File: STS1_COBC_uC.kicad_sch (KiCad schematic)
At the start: 46 parts, among them J16 SWD, U18 STWD100PYW83F, U19 STM32F411RET6TR, U28 MCP130T-300I_TT, U29 74LVC1G08GV,125, U31 74LVC1G08GV,125, U32 74LVC1G32GV,125, Y1 12M

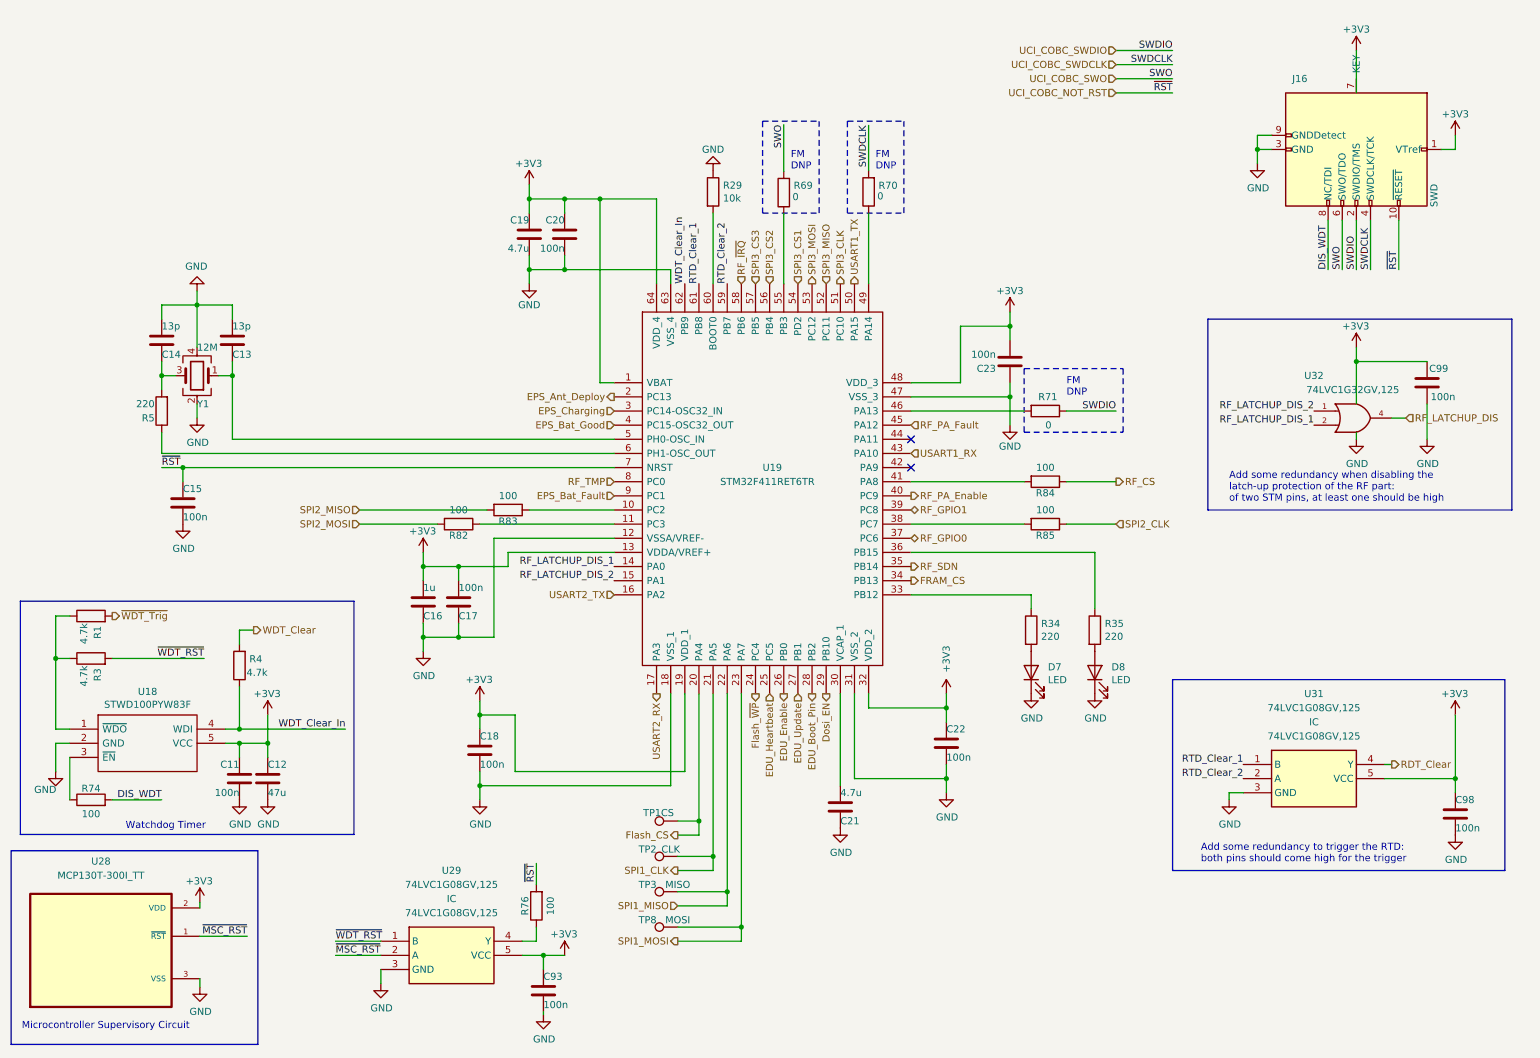
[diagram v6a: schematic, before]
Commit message: Fix power domain crossing issue between COBC and EPS
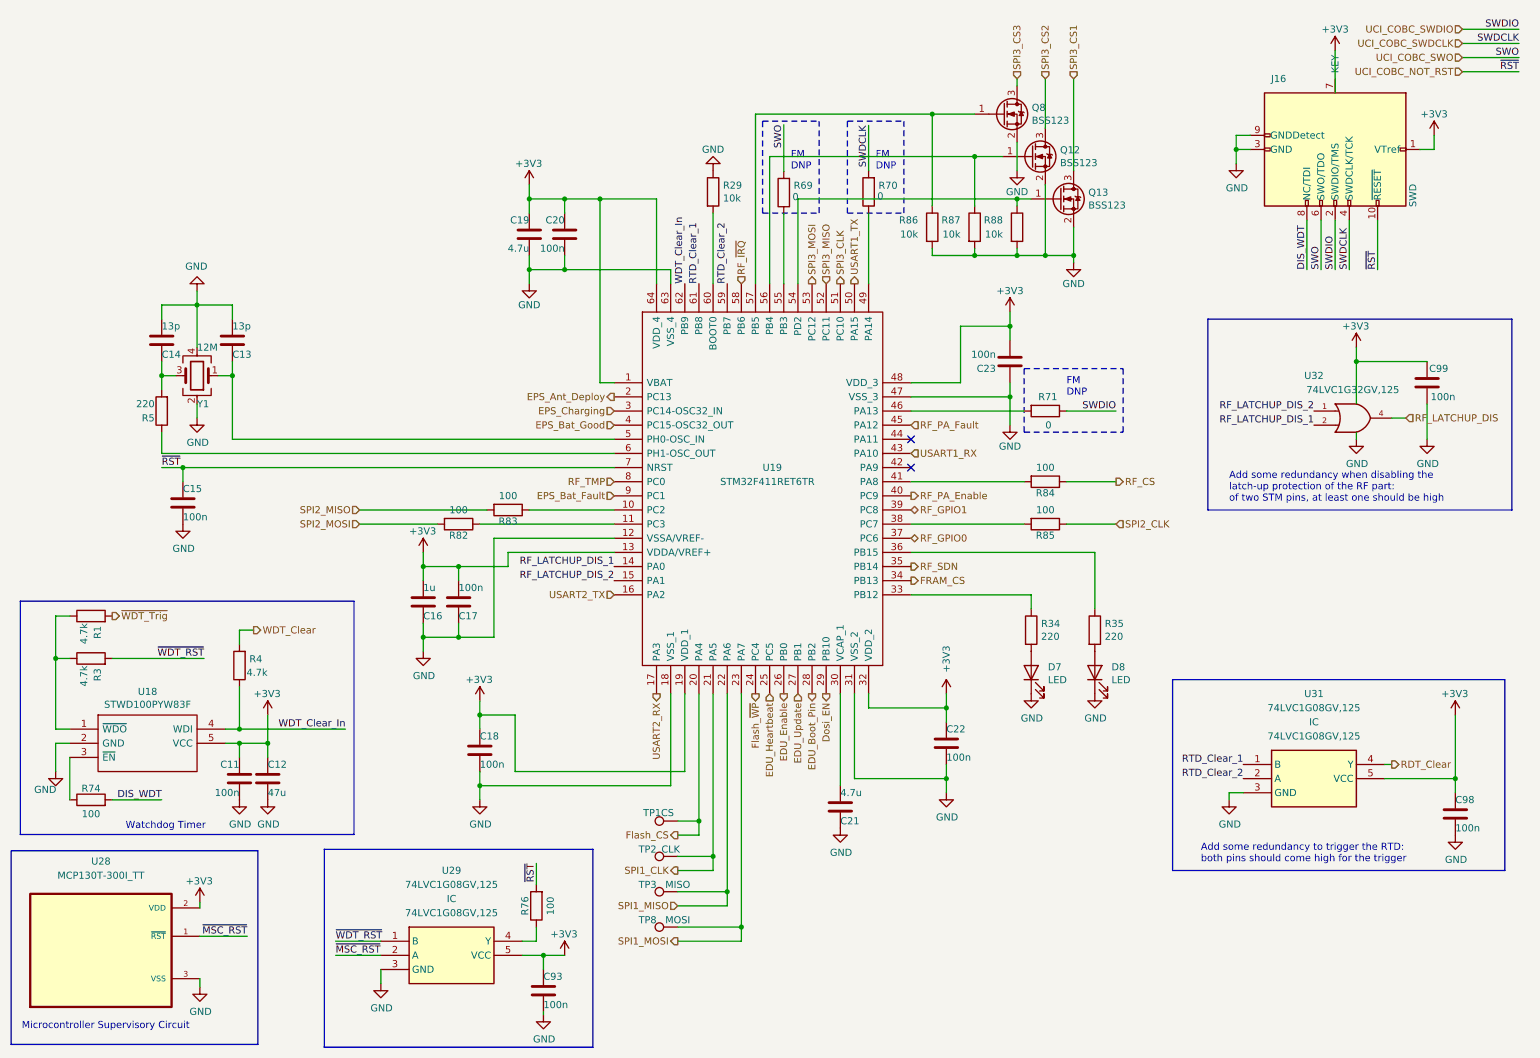
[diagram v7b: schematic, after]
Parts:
- added Q12, Q13, Q8: BSS123, Package_TO_SOT_SMD:SOT-23, symbol Device:Q_NMOS_GSD
- added R86, R87, R88: 10k, Resistor_SMD:R_0603_1608Metric, symbol Device:R
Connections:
- net GND: now also Q12.2 (S), Q13.2 (S), Q8.2 (S), R86.2, R87.2, R88.2
- net SPI3_CS1: now also Q13.3 (D); no longer U19.54 (PD2)
- net SPI3_CS2: now also Q12.3 (D); no longer U19.56 (PB4)
- net SPI3_CS3: now also Q8.3 (D); no longer U19.57 (PB5)
- new net: Q13.1 (G), R88.1, U19.54 (PD2)
- new net: Q12.1 (G), R87.1, U19.56 (PB4)
- new net: Q8.1 (G), R86.1, U19.57 (PB5)
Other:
- moved on the sheet: J16
